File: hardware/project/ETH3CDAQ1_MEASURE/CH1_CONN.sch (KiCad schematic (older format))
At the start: 1 part, among them J1101 Conn_02x10_Odd_Even

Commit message: PCB layout
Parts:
- renumbered J1101 to J1201
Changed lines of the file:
@@
 $Descr A4 11693 8268
 encoding utf-8
-Sheet 11 15
+Sheet 12 15
 Title ""
 Date ""
@@
 P 5450 2450
 AR Path="/5FC84995/5FDFC7E3" Ref="J?"  Part="1"
-AR Path="/5FDF6197/5FDFC7E3" Ref="J1101"  Part="1"
-F 0 "J1101" H 5500 3067 50  0000 C CNN
+AR Path="/5FDF6197/5FDFC7E3" Ref="J1201"  Part="1"
+F 0 "J1201" H 5500 3067 50  0000 C CNN
 F 1 "Conn_02x10_Odd_Even" H 5500 2976 50  0000 C CNN
 F 2 "Connector_PinSocket_2.54mm:PinSocket_2x10_P2.54mm_Vertical" H 5450 2450 50  0001 C CNN
@@
 $EndComp
 $Comp
-L power:GND #PWR01102
+L power:GND #PWR01202
 U 1 1 5FDFF3CF
 P 5250 2150
-F 0 "#PWR01102" H 5250 1900 50  0001 C CNN
+F 0 "#PWR01202" H 5250 1900 50  0001 C CNN
 F 1 "GND" V 5250 2000 50  0000 R CNN
 F 2 "" H 5250 2150 50  0001 C CNN
@@
 $EndComp
 $Comp
-L power:GND #PWR01103
+L power:GND #PWR01203
 U 1 1 5FDFF6AF
 P 5250 2250
-F 0 "#PWR01103" H 5250 2000 50  0001 C CNN
+F 0 "#PWR01203" H 5250 2000 50  0001 C CNN
 F 1 "GND" V 5250 2100 50  0000 R CNN
 F 2 "" H 5250 2250 50  0001 C CNN
@@
 $EndComp
 $Comp
-L power:GND #PWR01108
+L power:GND #PWR01208
 U 1 1 5FDFF8A2
 P 5750 2250
-F 0 "#PWR01108" H 5750 2000 50  0001 C CNN
+F 0 "#PWR01208" H 5750 2000 50  0001 C CNN
 F 1 "GND" V 5750 2100 50  0000 R CNN
 F 2 "" H 5750 2250 50  0001 C CNN
@@
 $EndComp
 $Comp
-L power:GND #PWR01101
+L power:GND #PWR01201
 U 1 1 5FE0131C
 P 5250 2050
-F 0 "#PWR01101" H 5250 1800 50  0001 C CNN
+F 0 "#PWR01201" H 5250 1800 50  0001 C CNN
 F 1 "GND" V 5250 1900 50  0000 R CNN
 F 2 "" H 5250 2050 50  0001 C CNN
@@
 	5800 2450 5850 2450
 $Comp
-L power:GND #PWR01104
+L power:GND #PWR01204
 U 1 1 5FE0A1DF
 P 5250 2650
-F 0 "#PWR01104" H 5250 2400 50  0001 C CNN
+F 0 "#PWR01204" H 5250 2400 50  0001 C CNN
 F 1 "GND" V 5250 2500 50  0000 R CNN
 F 2 "" H 5250 2650 50  0001 C CNN
@@
 $EndComp
 $Comp
-L power:GND #PWR01109
+L power:GND #PWR01209
 U 1 1 5FE0A3CB
 P 5750 2650
-F 0 "#PWR01109" H 5750 2400 50  0001 C CNN
+F 0 "#PWR01209" H 5750 2400 50  0001 C CNN
 F 1 "GND" V 5750 2500 50  0000 R CNN
 F 2 "" H 5750 2650 50  0001 C CNN
@@
 $EndComp
 $Comp
-L power:+3.3V #PWR01105
+L power:+3.3V #PWR01205
 U 1 1 5FE0C8F7
 P 5250 2750
-F 0 "#PWR01105" H 5250 2600 50  0001 C CNN
+F 0 "#PWR01205" H 5250 2600 50  0001 C CNN
 F 1 "+3.3V" V 5250 2900 50  0000 L CNN
 F 2 "" H 5250 2750 50  0001 C CNN
@@
 $EndComp
 $Comp
-L power:+3.3V #PWR01110
+L power:+3.3V #PWR01210
 U 1 1 5FE0CC32
 P 5750 2750
-F 0 "#PWR01110" H 5750 2600 50  0001 C CNN
+F 0 "#PWR01210" H 5750 2600 50  0001 C CNN
 F 1 "+3.3V" V 5750 2900 50  0000 L CNN
 F 2 "" H 5750 2750 50  0001 C CNN
@@
 $EndComp
 $Comp
-L power:+9V #PWR01106
+L power:+9V #PWR01206
 U 1 1 5FE0E9E2
 P 5250 2850
-F 0 "#PWR01106" H 5250 2700 50  0001 C CNN
+F 0 "#PWR01206" H 5250 2700 50  0001 C CNN
 F 1 "+9V" V 5250 3000 50  0000 L CNN
 F 2 "" H 5250 2850 50  0001 C CNN
@@
 $EndComp
 $Comp
-L power:+5V #PWR01111
+L power:+5V #PWR01211
 U 1 1 5FE0F294
 P 5750 2850
-F 0 "#PWR01111" H 5750 2700 50  0001 C CNN
+F 0 "#PWR01211" H 5750 2700 50  0001 C CNN
 F 1 "+5V" V 5750 3000 50  0000 L CNN
 F 2 "" H 5750 2850 50  0001 C CNN
@@
 $EndComp
 $Comp
-L ETH3CDAQ1:-18V #PWR01107
+L ETH3CDAQ1:-18V #PWR01207
 U 1 1 5FE10CD8
 P 5250 2950
-F 0 "#PWR01107" H 5250 2800 50  0001 C CNN
+F 0 "#PWR01207" H 5250 2800 50  0001 C CNN
 F 1 "-18V" V 5250 3100 50  0000 L CNN
 F 2 "" H 5250 2950 50  0001 C CNN
@@
 $EndComp
 $Comp
-L ETH3CDAQ1:+18V #PWR01112
+L ETH3CDAQ1:+18V #PWR01212
 U 1 1 5FE1185D
 P 5750 2950
-F 0 "#PWR01112" H 5750 2800 50  0001 C CNN
+F 0 "#PWR01212" H 5750 2800 50  0001 C CNN
 F 1 "+18V" V 5750 3100 50  0000 L CNN
 F 2 "" H 5750 2950 50  0001 C CNN

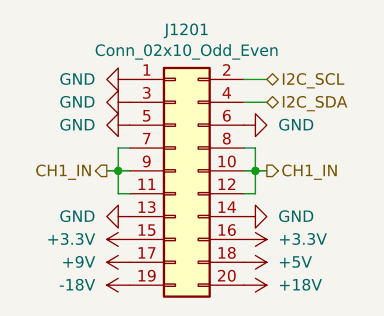
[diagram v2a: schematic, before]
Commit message: Started development of first current measurement module. Added CAN to the DAQ module.
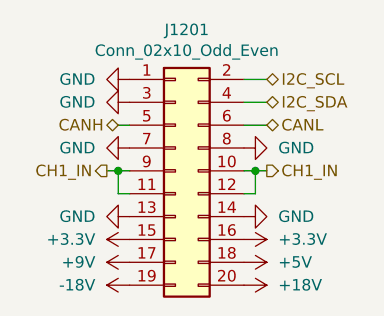
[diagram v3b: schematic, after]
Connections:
- net CH1_IN: no longer J1201.7 (Pin_7), J1201.8 (Pin_8)
- net GND: now also J1201.7 (Pin_7), J1201.8 (Pin_8); no longer J1201.5 (Pin_5), J1201.6 (Pin_6)
- new net CANH: J1201.5 (Pin_5)
- new net CANL: J1201.6 (Pin_6)
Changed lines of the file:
@@
-$EndComp
-$Comp
-L power:GND #PWR01203
-U 1 1 5FDFF6AF
-P 5250 2250
-F 0 "#PWR01203" H 5250 2000 50  0001 C CNN
-F 1 "GND" V 5250 2100 50  0000 R CNN
-F 2 "" H 5250 2250 50  0001 C CNN
-F 3 "" H 5250 2250 50  0001 C CNN
-	1    5250 2250
-	0    1    1    0
-$EndComp
-$Comp
-L power:GND #PWR01208
-U 1 1 5FDFF8A2
-P 5750 2250
-F 0 "#PWR01208" H 5750 2000 50  0001 C CNN
-F 1 "GND" V 5750 2100 50  0000 R CNN
-F 2 "" H 5750 2250 50  0001 C CNN
-F 3 "" H 5750 2250 50  0001 C CNN
-	1    5750 2250
-	0    -1   -1   0
 $EndComp
 $Comp
@@
 	5750 2050 5850 2050
 Wire Wire Line
-	5750 2350 5800 2350
-Wire Wire Line
-	5800 2350 5800 2450
-Wire Wire Line
 	5800 2550 5750 2550
 Wire Wire Line
@@
 Wire Wire Line
 	5800 2450 5800 2550
-Wire Wire Line
-	5250 2350 5200 2350
-Wire Wire Line
-	5200 2350 5200 2450
 Wire Wire Line
 	5200 2550 5250 2550
@@
 	0    1    1    0
 $EndComp
+Text HLabel 5200 2250 0    50   BiDi ~ 0
+CANH
+Text HLabel 5850 2250 2    50   BiDi ~ 0
+CANL
+Wire Wire Line
+	5200 2250 5250 2250
+Wire Wire Line
+	5850 2250 5750 2250
+$Comp
+L power:GND #PWR01203
+U 1 1 5FE56589
+P 5250 2350
+F 0 "#PWR01203" H 5250 2100 50  0001 C CNN
+F 1 "GND" V 5250 2200 50  0000 R CNN
+F 2 "" H 5250 2350 50  0001 C CNN
+F 3 "" H 5250 2350 50  0001 C CNN
+	1    5250 2350
+	0    1    1    0
+$EndComp
+$Comp
+L power:GND #PWR01208
+U 1 1 5FE567C2
+P 5750 2350
+F 0 "#PWR01208" H 5750 2100 50  0001 C CNN
+F 1 "GND" V 5750 2200 50  0000 R CNN
+F 2 "" H 5750 2350 50  0001 C CNN
+F 3 "" H 5750 2350 50  0001 C CNN
+	1    5750 2350
+	0    -1   -1   0
+$EndComp
 $EndSCHEMATC
